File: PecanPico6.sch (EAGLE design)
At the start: 79 parts, among them IC1 TPS79718DCKT, IC2 SI4463/4, IC3 UBLOX_MAX-6, IC4 LPC1114FHN33/333, IC5 SPV1040, IC6 AS213-92LF, IC7 BMP180, Q2 AP2301

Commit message: Created version 6b Removed RX part Removed UART pinheader below GPS module Enlarged Solar pad Fixed VCC_IO pin connection at GPS Enlarged Board for holes
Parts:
- removed C27, C4: 4.7pF, sven:CAP-0402
- removed C3: CAP-0402, sven:CAP-0402
- removed IC6: AS213-92LF, sven:AS213-92LF
- removed L6, L7: 56nH, sven:IND-0402
- removed L8: IND-0402, sven:IND-0402
- removed R19: RES-0402, sven:RES-0402
- removed U$3: JTI_ANTENNA-1575AT43A40, ava:JTI_ANTENNA-1575AT43A40
- removed UART: PINHEAD_PINHD-1X10S, 1_27x3:PINHEAD_PINHD-1X10S
- added JP1: GPSANTENNA, sven:M01SOLAR
- C1, C17: MF (none) -> ILLINOIS CAPACITOR,INC.; MPN (none) -> 225CKH250M; OC_NEWARK (none) -> 69K7918
- C10, C11, C12, C13, C14, C15, C16, C18, C19, C2, C20, C21, C22, C24, C25, C5, C6, C7, C9, IC4, JP2, JP3, JP4, JP5, L1, L2, L3, L4, L5, Q2, R1, R10, R11, R12, R13, R15, R16, R17, R18, R2, R3, R4, R5, R6, R7, R8, R9, SJ7, SJ8, TP1, TP2, U$1: OC_NEWARK (none) -> unknown
- IC1: MF (none) -> TEXAS INSTRUMENTS
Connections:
- removed net GND: C1.1, C11.1, C12.1, C13.1, C14.1, C15.2, C16.2, C17.2, C18.1, C2.1, C20.1, C21.1, C25.1, C27.2, C5.1, C6.1, C7.1, C9.1, IC1.GND, IC2.18_GNDX, IC2.5_NC, IC2.GND, IC3.10_GND, IC3.12_GND, IC3.1_GND, IC4.GND, IC5.GND, IC6.GND, IC7.GND, JP2.10, JP5.10, JP5.11, JP5.12, JP5.3, R12.1, R13.1, R18.1, R19.1, R2.1, R9.1, TP2.TP, U$1.GND1, U$1.GND2, U$1.GND3, UART.3, VCXO.GND
- removed net N$16: C3.1, L8.1, R19.2
- removed net N$24: C4.1, IC2.2_RXP, L6.2
- removed net N$33: C27.1, IC2.3_RXN, L6.1, L7.1
- removed net N$37: C4.2, IC6.B1, L7.2
- removed net N$5: C25.2, IC3.8_VCC, Q2.D, SJ5.1
- new net N$100: C1.1, C11.1, C12.1, C13.1, C14.1, C15.2, C16.2, C17.2, C18.1, C2.1, C20.1, C21.1, C25.1, C5.1, C6.1, C7.1, C9.1, IC1.GND, IC2.18_GNDX, IC2.5_NC, IC2.GND, IC3.10_GND, IC3.12_GND, IC3.1_GND, IC4.GND, IC5.GND, IC7.GND, JP2.10, JP5.10, JP5.11, JP5.12, JP5.3, R12.1, R13.1, R18.1, R2.1, R9.1, TP2.TP, U$1.GND1, U$1.GND2, U$1.GND3, VCXO.GND
- net N$1: now also L3.1; no longer IC6.A1
- net N$11: now also C25.2, IC3.7_VCC_IO, IC3.8_VCC, Q2.D, SJ5.1; no longer IC6.B2, L3.1
- net N$27: no longer C3.2, L8.2
- net N$3: now also JP1.1; no longer U$3.FEED
- net RXD: no longer UART.2
- net RX_EN: no longer IC6.V2
- net TXD: no longer UART.1
- net TX_EN: no longer IC6.V1
- net VCC15: no longer IC3.7_VCC_IO
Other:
- moved on the sheet: C2, C5, C7, IC7, L2

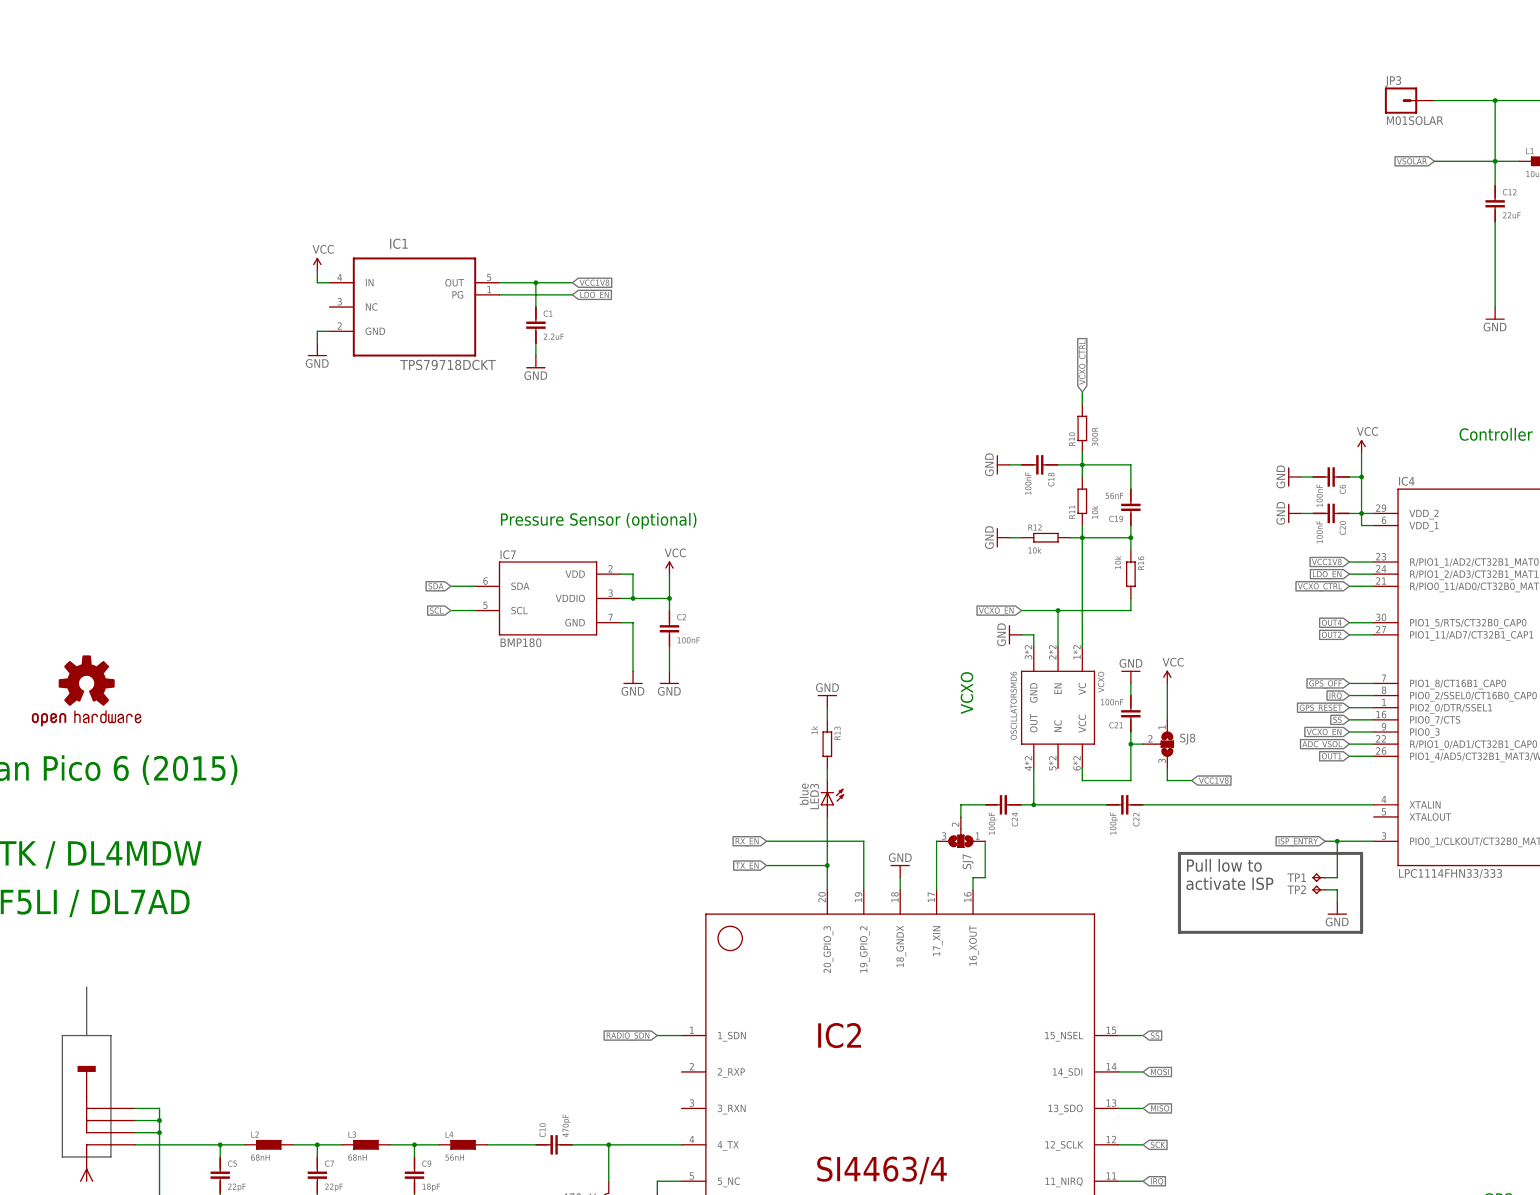
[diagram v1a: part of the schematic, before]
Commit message: Moved solar pads
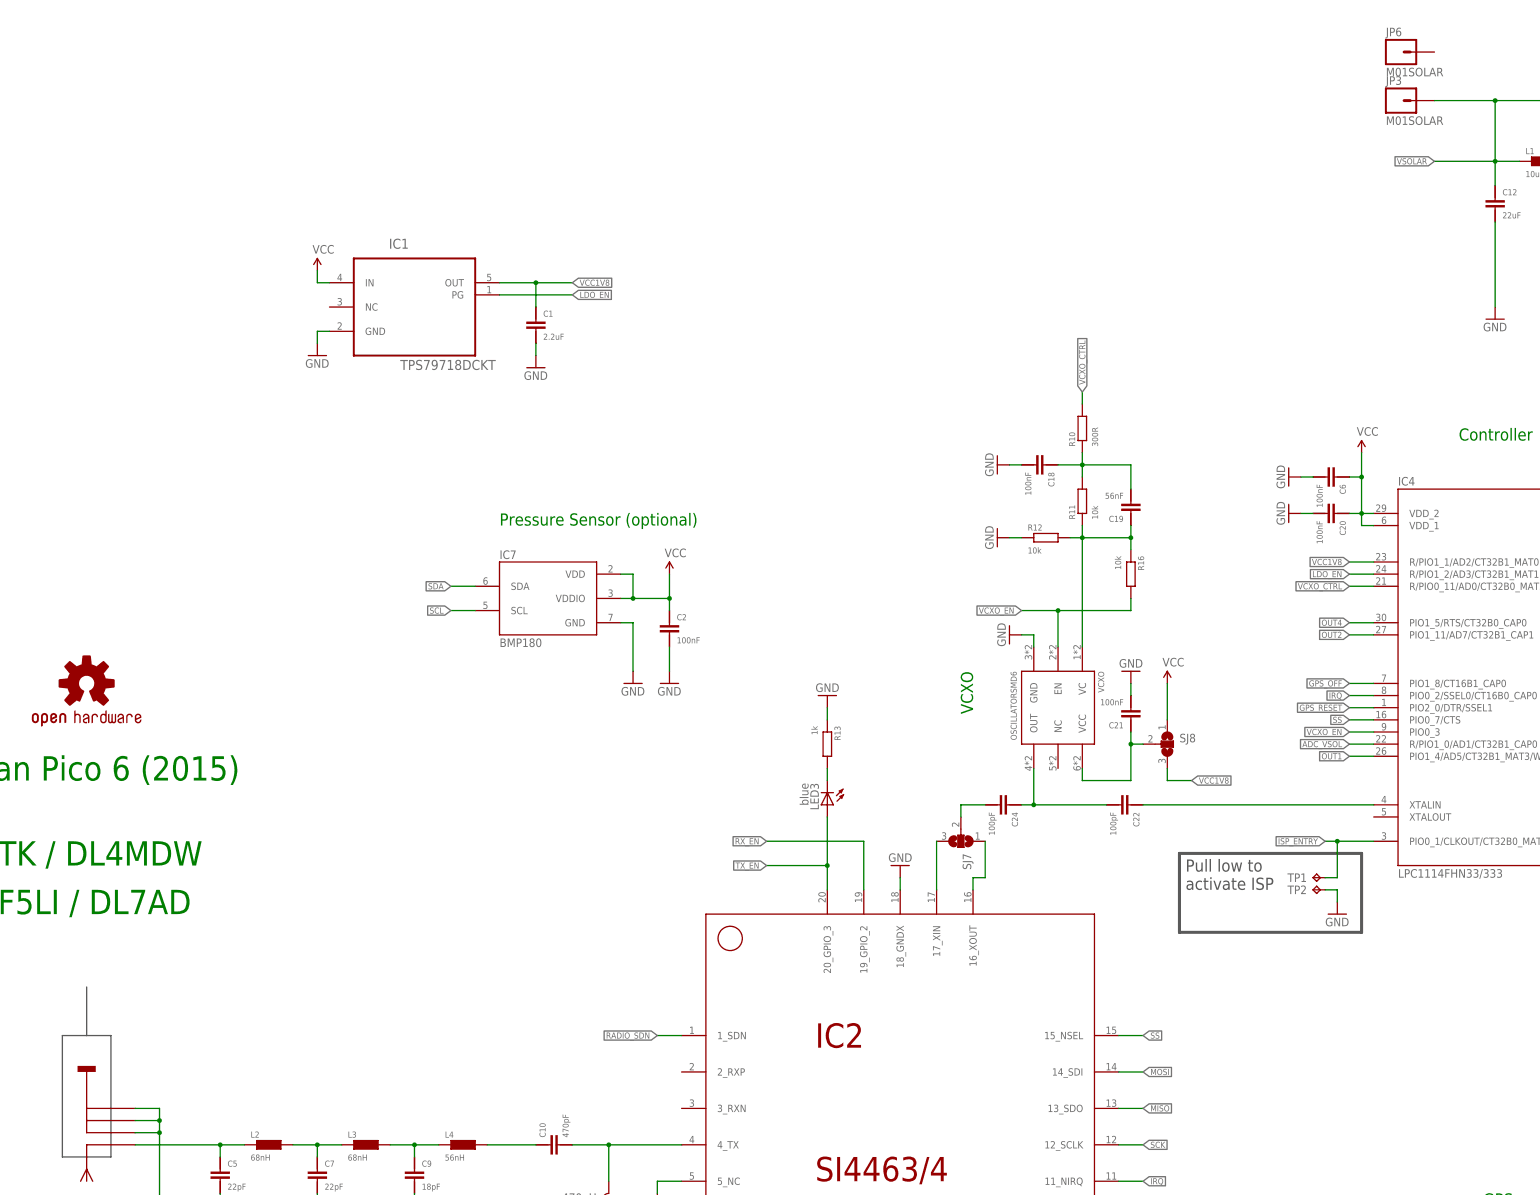
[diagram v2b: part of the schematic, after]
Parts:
- added JP6: M01SOLAR, sven:M01SOLAR
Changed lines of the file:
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@@
+<attribute name="OC_NEWARK" value="unknown"/>
+</part>
+<part name="JP6" library="sven" deviceset="M01" device="SOLAR">
+<attribute name="MF" value=""/>
+<attribute name="MPN" value=""/>
 <attribute name="OC_NEWARK" value="unknown"/>
 </part>
@@
 <attribute name="MPN" x="276.86" y="78.74" size="1.778" layer="96" display="off"/>
 </instance>
+<instance part="JP6" gate="G$1" x="297.18" y="332.74">
+<attribute name="OC_NEWARK" x="297.18" y="332.74" size="1.778" layer="96" display="off"/>
+<attribute name="MF" x="297.18" y="332.74" size="1.778" layer="96" display="off"/>
+<attribute name="MPN" x="297.18" y="332.74" size="1.778" layer="96" display="off"/>
+</instance>
 </instances>
